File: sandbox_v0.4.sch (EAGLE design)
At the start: 71 parts, among them J1 CON_MOLEX_2V, J2 UART, J3 CON_MICROSD-SFE, J5 JTAG, J8 CON_USB_A_DUAL, U2 W65C02S44PLCC-SOCKET, U3 XC6SLX9-2TQC144C, U4 MT48LC64M8, U5 M25P80-VMN6P

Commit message: connected CPU and FPGA
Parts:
- U2: value W65C02S44PLCC-SOCKET -> 65C02/65C816
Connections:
- removed net N$13: U2.10A0
- removed net N$14: U2.11A1
- removed net N$15: U2.13A2
- removed net N$16: U2.14A3
- removed net N$18: U2.15A4
- removed net N$19: U2.16A5
- removed net N$20: U2.17A6
- removed net N$21: U2.18A7
- removed net N$22: U2.19A8
- removed net N$23: U2.20A9
- removed net N$24: U2.21A10
- removed net N$25: U2.22A11
- removed net N$26: U2.25A12
- removed net N$27: U2.26A13
- removed net N$28: U2.27A14
- removed net N$29: U2.28A15
- removed net N$30: U2.36D0
- removed net N$31: U2.35D1
- removed net N$32: U2.34D2
- removed net N$33: U2.33D3
- removed net N$34: U2.32D4
- removed net N$35: U2.31D5
- removed net N$36: U2.30D6
- removed net N$37: U2.29D7
- removed net N$38: U2.44RESB
- removed net N$39: U2.5IRQB
- removed net N$40: U2.7NMIB
- removed net N$41: U2.8SYNC
- removed net N$43: U2.3RDY
- removed net N$44: U2.2VPB
- removed net N$47: U2.38RWB
- removed net N$49: U2.43PHI2O
- removed net N$50: U2.41PHI2
- removed net N$56: U2.4PHI1O
- removed net RES: R4.1, U3.P144
- new net CPU_A0: U2.10A0, U3.P131
- new net CPU_A1: U2.11A1, U3.P126
- new net CPU_A10: U2.21A10, U3.P105
- new net CPU_A11: U2.22A11, U3.P97
- new net CPU_A12: U2.25A12, U3.P104
- new net CPU_A13: U2.26A13, U3.P98
- new net CPU_A14: U2.27A14, U3.P102
- new net CPU_A15: U2.28A15, U3.P99
- new net CPU_A2: U2.13A2, U3.P121
- new net CPU_A3: U2.14A3, U3.P120
- new net CPU_A4: U2.15A4, U3.P117
- new net CPU_A5: U2.16A5, U3.P116
- new net CPU_A6: U2.17A6, U3.P112
- new net CPU_A7: U2.18A7, U3.P94
- new net CPU_A8: U2.19A8, U3.P111
- new net CPU_A9: U2.20A9, U3.P95
- new net CPU_ABORT: U2.4PHI1O, U3.P140
- new net CPU_CLK: U2.41PHI2, U3.P132
- new net CPU_D0: U2.36D0, U3.P124
- new net CPU_D1: U2.35D1, U3.P123
- new net CPU_D2: U2.34D2, U3.P119
- new net CPU_D3: U2.33D3, U3.P118
- new net CPU_D4: U2.32D4, U3.P115
- new net CPU_D5: U2.31D5, U3.P114
- new net CPU_D6: U2.30D6, U3.P101
- new net CPU_D7: U2.29D7, U3.P100
- new net CPU_IRQ: U2.5IRQB, U3.P137
- new net CPU_NMI: U2.7NMIB, U3.P139
- new net CPU_RDY: U2.3RDY, U3.P134
- new net CPU_RES: R4.1, U2.44RESB, U3.P144
- new net CPU_RW: U2.38RWB, U3.P127
- new net CPU_VDA: U2.43PHI2O, U3.P133
- new net CPU_VP: U2.2VPB, U3.P141
- new net CPU_VPA: U2.8SYNC, U3.P138

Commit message: connected Video (mostly)
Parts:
- added C36: 12nF, c-scape:CAP0402-SMALL
- added C37: 150nF, c-scape:CAP0402-SMALL
- added C38: 2.2nF, c-scape:CAP0402-SMALL
- added C39: (no value), 00-own_parts:CAP0603
- added C41: 10U, 00-own_parts:CAP0603
- added CD1, CD2, CD3, CD4, CD5: 100n, c-scape:CAP0402-SMALL
- added J4: CON_USB_MINI, c-scape:CON_USB_MINI
- added J6: CON-VGA, c-scape:CON-VGA
- added J7: JACK_3.5MM_LUMBERG, c-scape:JACK_3.5MM_LUMBERG
- added L1: (no value), c-scape:BEAD0603
- added R10, R16, R26: 1K, c-scape:RES0402-SMALL
- added R11, R17, R27: 2K, c-scape:RES0402-SMALL
- added R18, R24, R28: 4.02K, c-scape:RES0402-SMALL
- added R25, R8, R9: 499R, c-scape:RES0402-SMALL
- added R29, R30: 100R, c-scape:RES0402-SMALL
- added R31: 170R, c-scape:RES0402-SMALL
- added R32: 150R, c-scape:RES0402-SMALL
- added R33, R34, R35: 75R, c-scape:RES0402-SMALL
- added R36, R37: (no value), c-scape:RES0402-SMALL
- added R5: 2.2K, c-scape:RES0402-SMALL
- added U1: ADV7391, c-scape:ADV7391
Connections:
- removed net USB+: U3.P59
- removed net USB-: U3.P58
- new net BLU0: R28.2, U1.CLKIN, U3.P79
- new net BLU1: R27.2, U3.P78
- new net BLU2: R26.2, U3.P75
- new net BLU3: R25.2, U3.P74
- new net GRN0: R24.2, U1.P4, U3.P83
- new net GRN1: R17.2, U1.P5, U3.P82
- new net GRN2: R16.2, U1.P6, U3.P81
- new net GRN3: R9.2, U1.P7, U3.P80
- new net HSYNC: R29.2, U1.!HSYNC, U3.P92
- new net N$1: C36.1, R31.1, U1.EXT_LF
- new net N$10: C37.1, R31.2
- new net N$11: C38.1, U1.COMP
- new net N$12: R32.1, U1.RSET
- new net N$13: J7.RED, R33.2, U1.DAC3/PR/CHROMA/R
- new net N$14: J7.BLU, R34.2, U1.DAC2/PB/LUMA/B
- new net N$15: J7.GRN, R35.2, U1.DAC1/Y/G/CVBS
- new net N$16: CD1.1, R36.2, U1.VDD@1
- new net N$17: CD3.1, R37.2, U1.VDD_IO
- new net RED0: R18.2, U1.P0, U3.P88
- new net RED1: R11.2, U1.P1, U3.P87
- new net RED2: R10.2, U1.P2, U3.P85
- new net RED3: R8.2, U1.P3, U3.P84
- new net SCL: U1.SCL/MOSI
- new net SDA: U1.SDA/SCLK
- new net SD_CS: J3.2CS
- new net SD_DI: J3.3DI
- new net SD_DO: J3.7DO
- new net SD_SCK: J3.5SCK
- new net VCC: C38.2, C39.1, CD2.1, L1.P$1, R36.1, R37.1, U1.VAA
- new net VDD_1V8: C36.2, C37.2, C41.1, CD4.1, CD5.1, U1.PVDD, U1.VDD
- new net VGA_BLU: J6.BLU+, R25.1, R26.1, R27.1, R28.1
- new net VGA_GRN: J6.GRN+, R16.1, R17.1, R24.1, R9.1
- new net VGA_HS: J6.HSYNC+, R29.1
- new net VGA_RED: J6.RED+, R10.1, R11.1, R18.1, R8.1
- new net VGA_VS: J6.VSYNC+, R30.1
- new net VSYNC: R30.2, U1.!VSYNC, U3.P93
- net CPU_RDY: now also R5.1
- net GND: now also C39.2, C41.2, CD1.2, CD2.2, CD3.2, CD4.2, CD5.2, J4.CASE, J6.BLU-, J6.GRN-, J6.HSYNC-, J6.RED-, J6.VSYNC-, J7.GND, R32.2, R33.1, R34.1, R35.1, U1.AGND, U1.ALSB/!SPI_SS, U1.DGND, U1.DGND@1, U1.GND_IO, U1.PGND
- net UART_RXD: no longer U3.P46
- net UART_TXD: no longer U3.P47
- net VDD_3V3: now also L1.P$2, R5.2
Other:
- note added: "151104"
- note added: "6502 sandbox - CPU and SDRAM"
- note removed: "130217"
- note removed: "6502 Sandbox - SDRAM"
- note removed: "6502 sandbox - CPU"

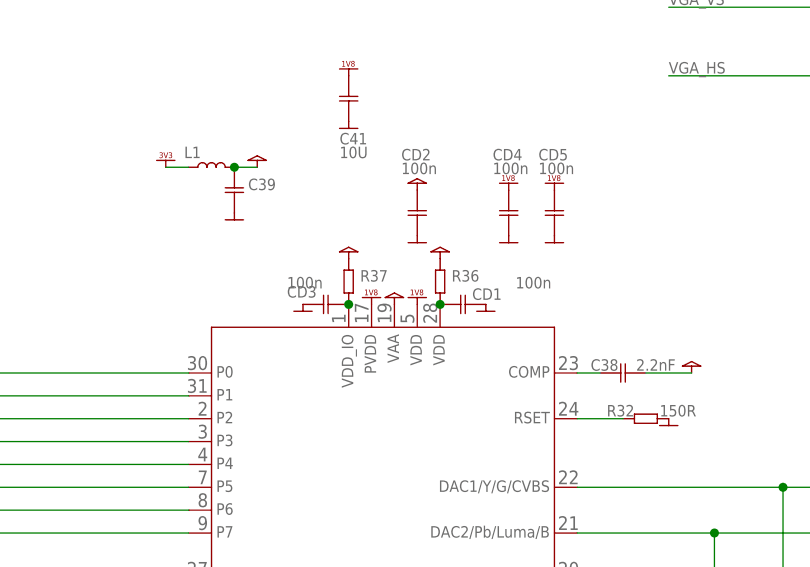
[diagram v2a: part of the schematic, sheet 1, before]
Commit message: fixed bead symbol
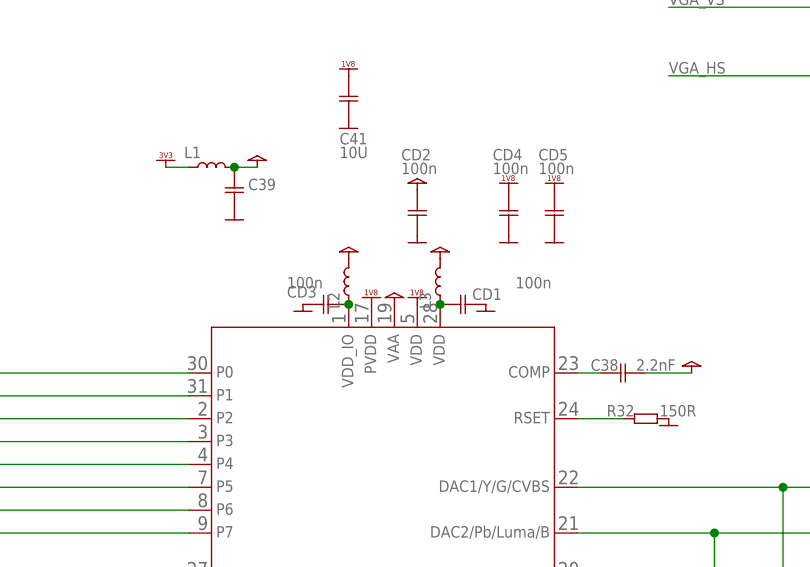
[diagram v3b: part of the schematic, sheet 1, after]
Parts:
- removed R36, R37: (no value), c-scape:RES0402-SMALL
- added L2, L3: (no value), c-scape:BEAD0402-SMALL
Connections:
- net N$16: now also L3.P$2; no longer R36.2
- net N$17: now also L2.P$2; no longer R37.2
- net VCC: now also L2.P$1, L3.P$1; no longer R36.1, R37.1
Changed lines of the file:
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@@
 <part name="U$198" library="c-scape" deviceset="VCC_1V8" device=""/>
 <part name="U$199" library="c-scape" deviceset="VCC_1V8" device=""/>
-<part name="R36" library="c-scape" deviceset="RES" device="0402-SMALL"/>
-<part name="U$187" library="00-own_parts" deviceset="VCC" device=""/>
-<part name="R37" library="c-scape" deviceset="RES" device="0402-SMALL"/>
 <part name="C41" library="00-own_parts" deviceset="CAP0603" device="" value="10U"/>
 <part name="U$200" library="00-own_parts" deviceset="GND" device=""/>
 <part name="U$190" library="c-scape" deviceset="VCC_1V8" device=""/>
+<part name="U$187" library="00-own_parts" deviceset="VCC" device=""/>
+<part name="L2" library="c-scape" deviceset="BEAD" device="0402-SMALL"/>
+<part name="L3" library="c-scape" deviceset="BEAD" device="0402-SMALL"/>
 </parts>
 <sheets>
@@
 <instance part="U$198" gate="G$1" x="96.52" y="96.52"/>
 <instance part="U$199" gate="G$1" x="101.6" y="96.52"/>
-<instance part="R36" gate="G$1" x="88.9" y="86.36" smashed="yes">
-<attribute name="NAME" x="90.17" y="86.36" size="1.27" layer="95" font="vector" ratio="10"/>
-<attribute name="VALUE" x="90.17" y="84.836" size="1.27" layer="96" font="vector" ratio="10"/>
-</instance>
-<instance part="U$187" gate="G$1" x="78.74" y="88.9"/>
-<instance part="R37" gate="G$1" x="78.74" y="86.36" smashed="yes">
-<attribute name="NAME" x="80.01" y="86.36" size="1.27" layer="95" font="vector" ratio="10"/>
-<attribute name="VALUE" x="80.01" y="84.836" size="1.27" layer="96" font="vector" ratio="10"/>
-</instance>
 <instance part="C41" gate="G$1" x="78.74" y="106.68" smashed="yes">
 <attribute name="NAME" x="77.724" y="101.6" size="1.27" layer="95" font="vector" ratio="10"/>
@@
 <instance part="U$200" gate="G$1" x="78.74" y="104.14"/>
 <instance part="U$190" gate="G$1" x="78.74" y="109.22"/>
+<instance part="U$187" gate="G$1" x="78.74" y="88.9"/>
+<instance part="L2" gate="L1" x="78.74" y="86.36" rot="R90"/>
+<instance part="L3" gate="L1" x="88.9" y="86.36" rot="R90"/>
 </instances>
 <busses>
@@
 </segment>
 <segment>
+<pinref part="U$187" gate="G$1" pin="VCC"/>
+<pinref part="L2" gate="L1" pin="P$1"/>
+</segment>
+<segment>
 <pinref part="U$178" gate="G$1" pin="VCC"/>
-<pinref part="R36" gate="G$1" pin="1"/>
-</segment>
-<segment>
-<pinref part="U$187" gate="G$1" pin="VCC"/>
-<pinref part="R37" gate="G$1" pin="1"/>
+<pinref part="L3" gate="L1" pin="P$1"/>
 </segment>
 </net>
@@
 <segment>
 <pinref part="U1" gate="A" pin="VDD@1"/>
-<pinref part="R36" gate="G$1" pin="2"/>
 <pinref part="CD1" gate="G$1" pin="1"/>
 <junction x="88.9" y="83.82"/>
 <pinref part="CD1" gate="G$1" pin="1"/>
+<pinref part="L3" gate="L1" pin="P$2"/>
 </segment>
 </net>
@@
 <pinref part="U1" gate="A" pin="VDD_IO"/>
 <pinref part="CD3" gate="G$1" pin="1"/>
-<pinref part="R37" gate="G$1" pin="2"/>
+<pinref part="L2" gate="L1" pin="P$2"/>
 <junction x="78.74" y="83.82"/>
-<pinref part="R37" gate="G$1" pin="2"/>
-</segment>
-</net>
+<pinref part="L2" gate="L1" pin="P$2"/>
+</segment>
+</net>

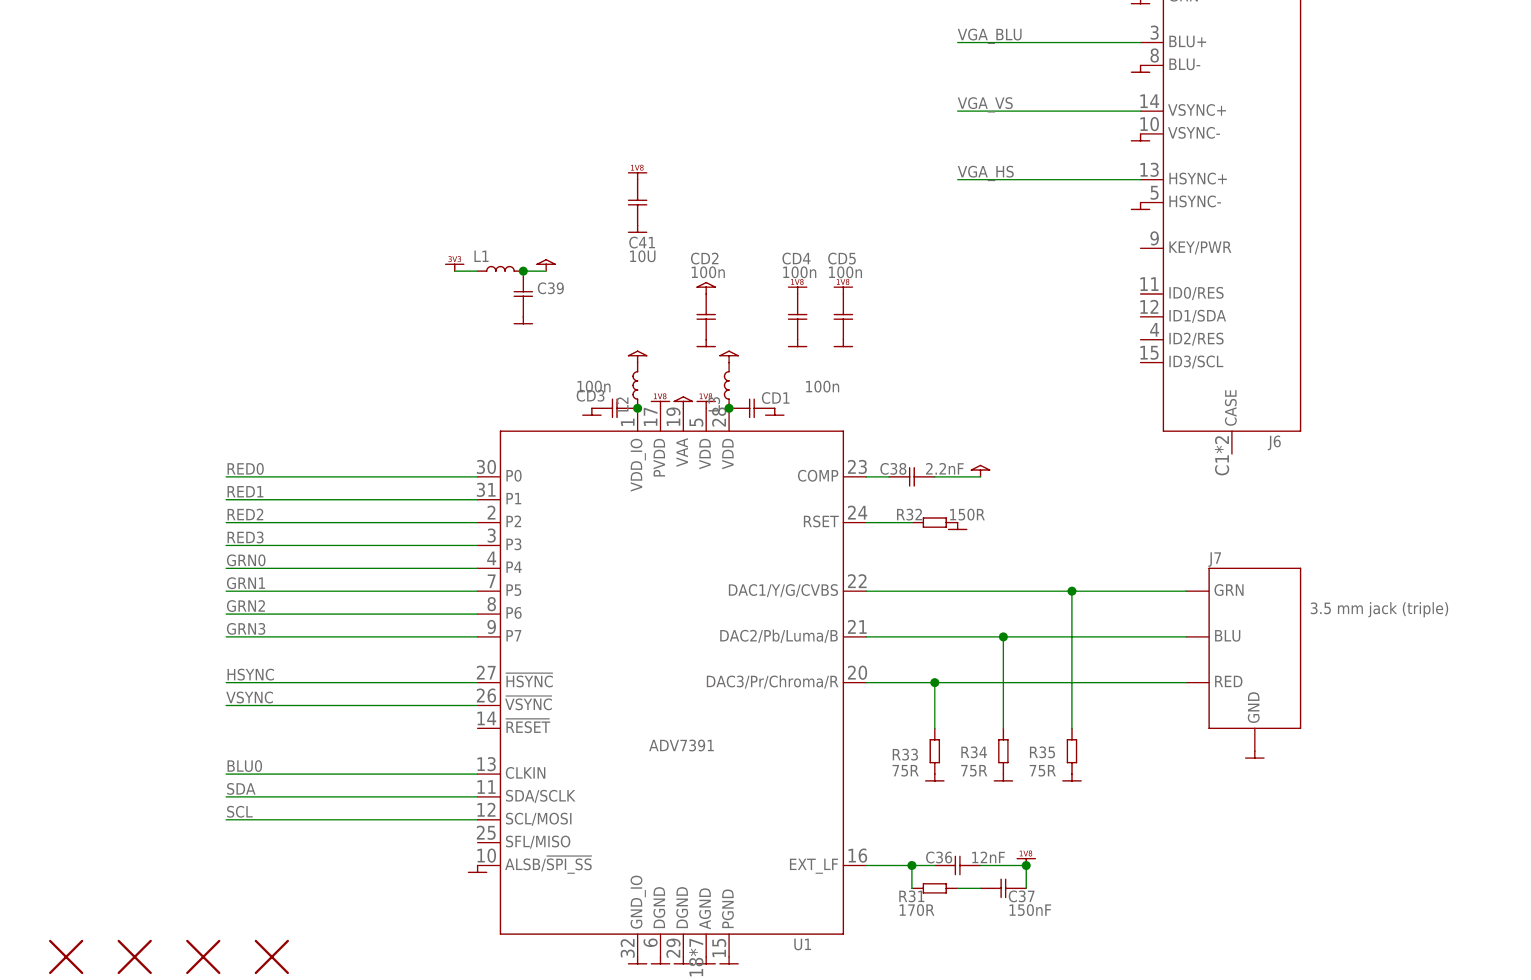
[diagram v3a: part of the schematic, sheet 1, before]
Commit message: add RC reset to video, cleanups
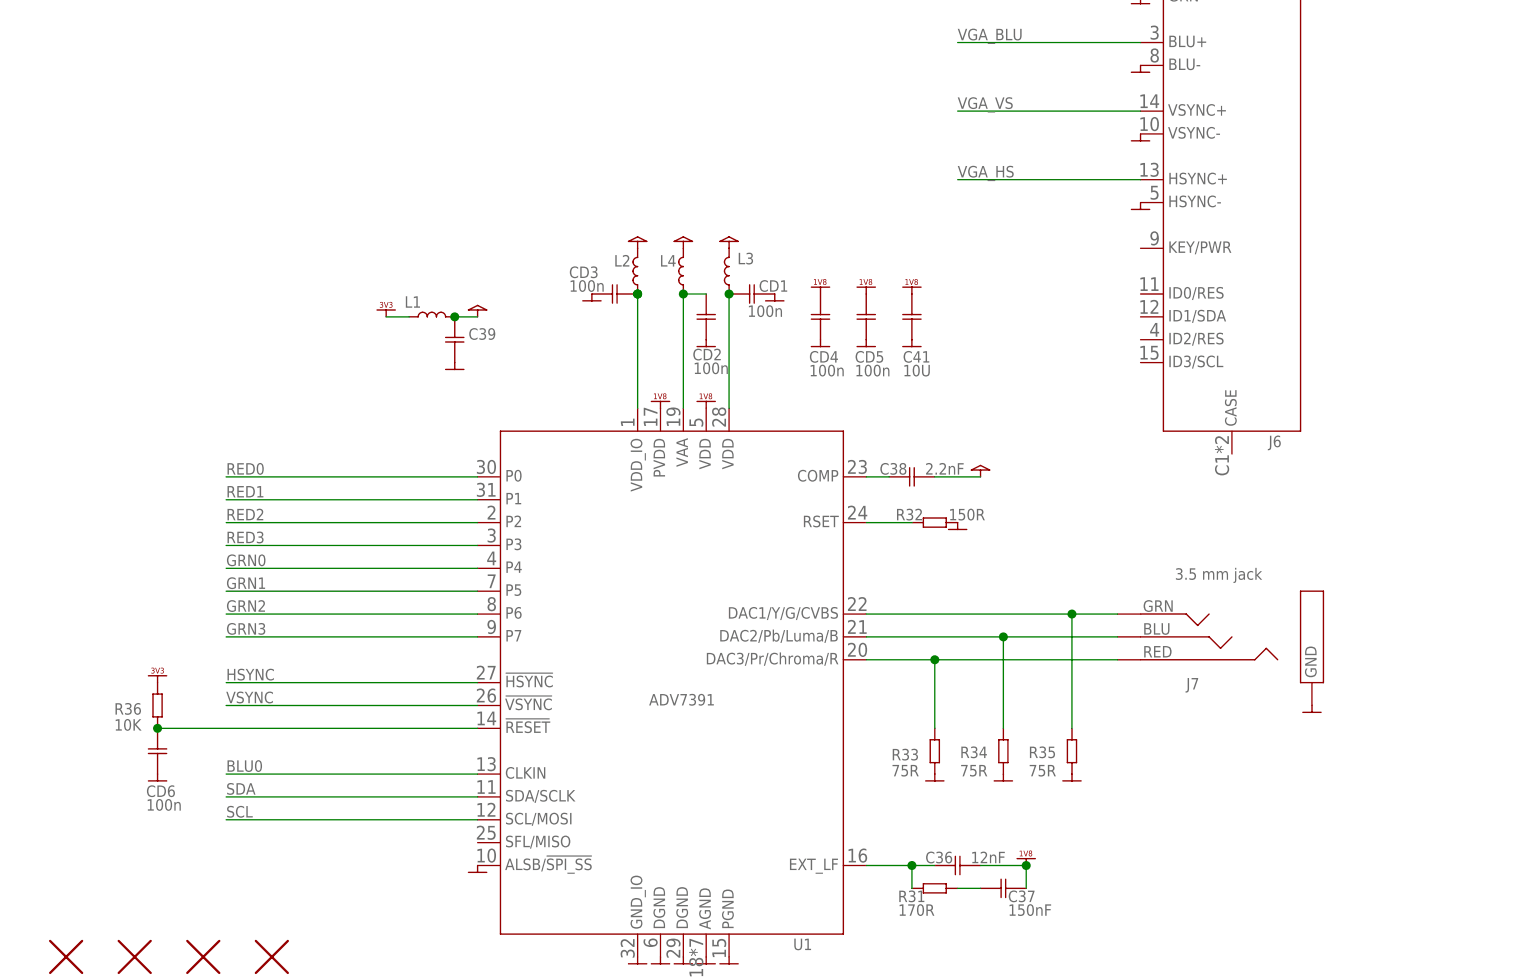
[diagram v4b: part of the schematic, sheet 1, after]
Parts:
- added CD6: 100n, c-scape:CAP0402-SMALL
- added L4: (no value), c-scape:BEAD0402-SMALL
- added R36: 10K, c-scape:RES0402-SMALL
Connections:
- net N$13 renamed RED
- net N$14 renamed BLUE
- net N$15 renamed GREEN
- new net N$13: CD2.1, L4.P$2, U1.VAA
- new net N$14: CD6.1, R36.1, U1.!RESET
- net GND: now also CD6.2
- net VCC: now also L4.P$1; no longer CD2.1, U1.VAA
- net VDD_3V3: now also R36.2
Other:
- moved on the sheet: C39, C41, CD1, CD3, CD4, CD5, L1, L2, L3
